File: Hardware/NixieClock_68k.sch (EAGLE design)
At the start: 80 parts, among them IC1 68008, IC10 7805, IC11 MIC803, IC2 AS6C1008, IC3 39SF020, IC4 DS1244Y, IC5 FT245R, IC6 NE555, IC7 ATF1504AS, IC8 74HC377N, IC9 74HC373N, Q1 2N4401

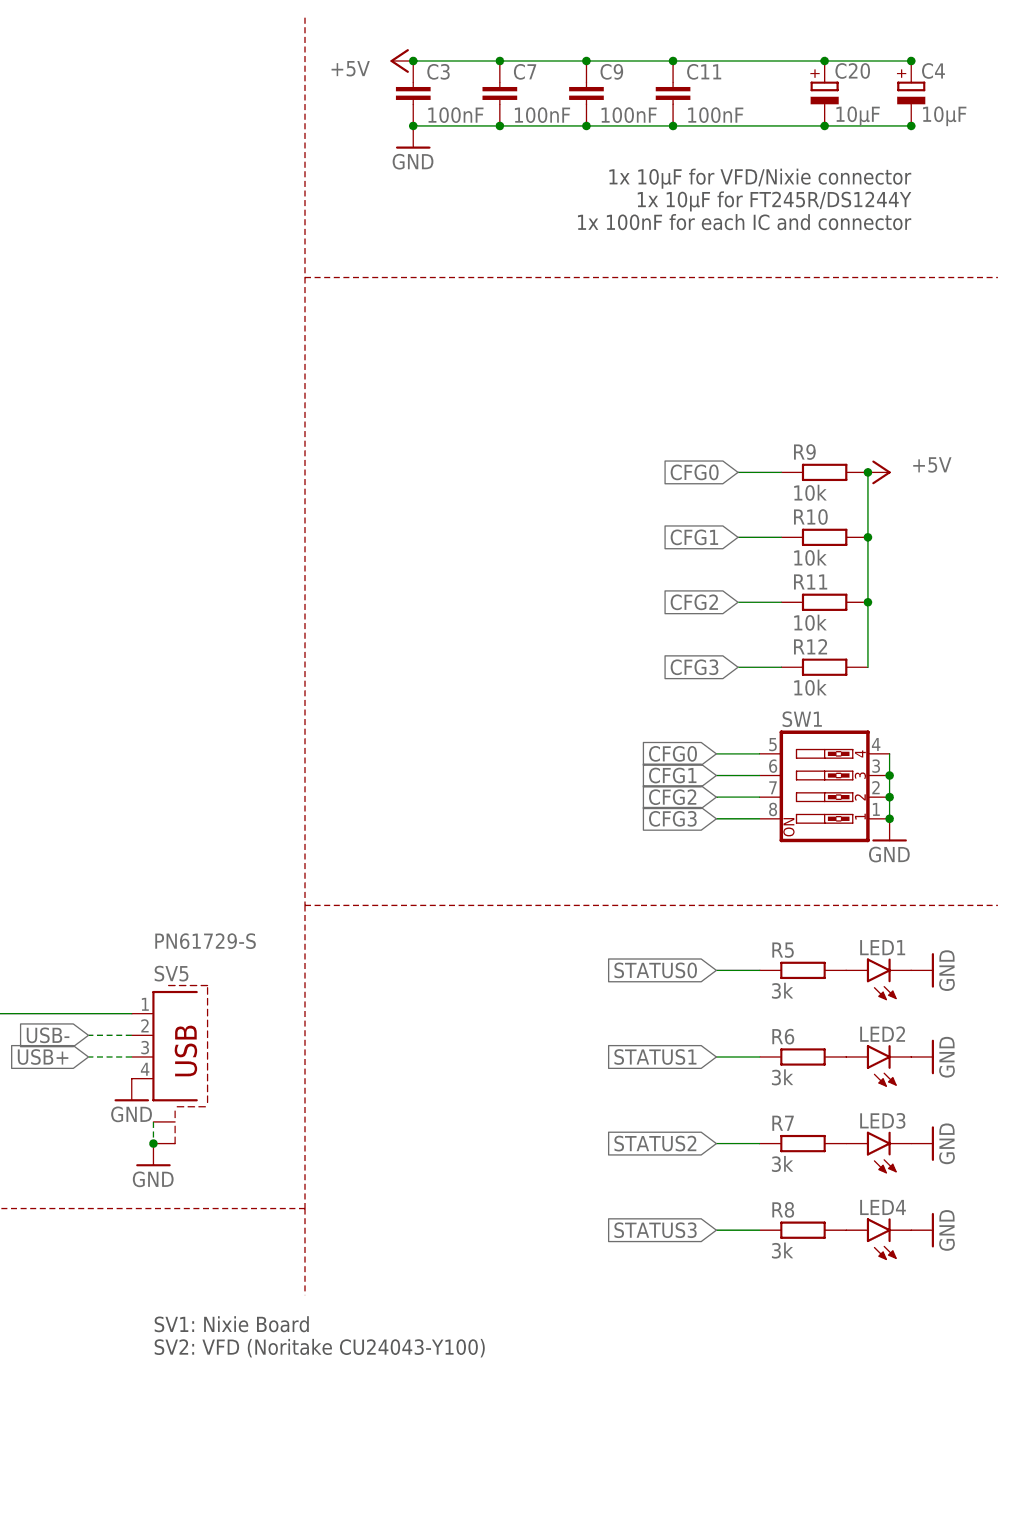
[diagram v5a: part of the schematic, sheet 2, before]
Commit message: more progress routing board
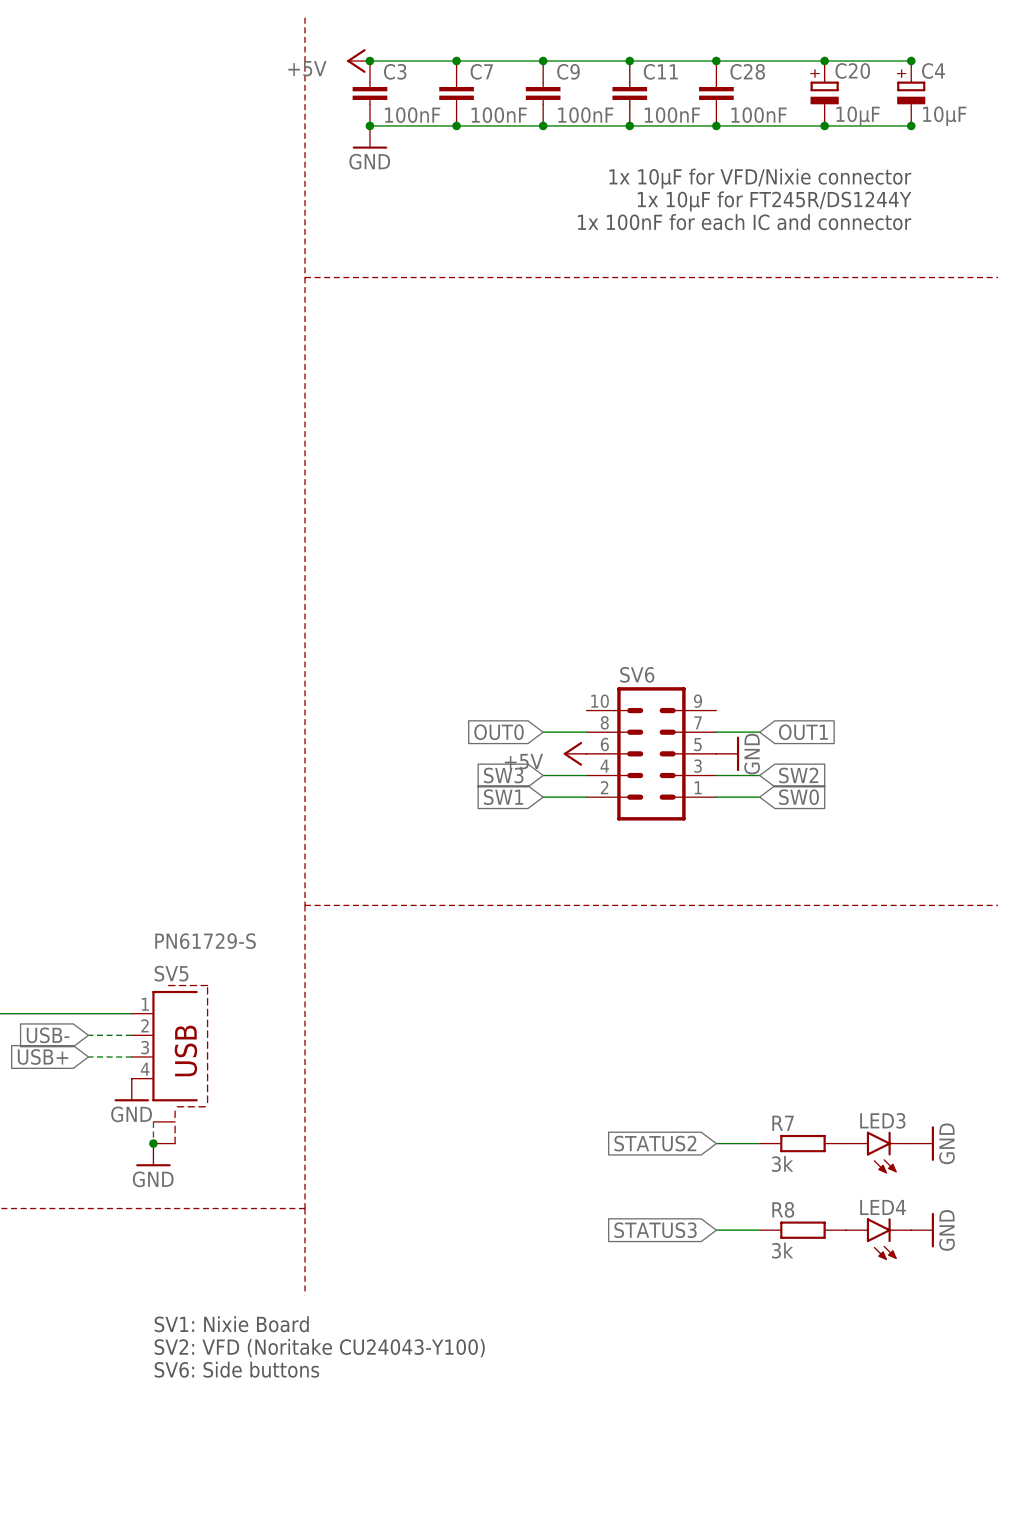
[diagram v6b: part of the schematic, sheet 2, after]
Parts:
- removed D1: 1N4148, diode:1N4148DO35-7
- removed LED1, LED2: (no value), led:LEDCHIPLED_1206
- removed Q1: 2N4401, transistor-npn:2N4416
- removed R10, R11, R12, R9: 10k, rcl:R-EU_R2012
- removed R24, R25: 1k, rcl:R-EU_R2012
- removed R5, R6: 3k, rcl:R-EU_R2012
- removed SP1: KSS1201, buzzer:KSS1201
- removed SW1: (no value), special:SW_DIP-4
- added C28: 100nF, rcl:C-EUC0805
- added SV6: (no value), con-lstb:MA05-2
- renumbered QG1 to X1
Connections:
- removed net !IO_OUT_EN: IC7.IO25
- removed net BEEPER: IC8A.7Q, R24.1
- removed net CFG0: IC9A.5D, R9.1, SW1.5
- removed net CFG1: IC9A.6D, R10.1, SW1.6
- removed net CFG2: IC9A.7D, R11.1, SW1.7
- removed net CFG3: IC9A.8D, R12.1, SW1.8
- removed net JTAG_TCK: IC7.TCK
- removed net JTAG_TDI: IC7.TDI
- removed net JTAG_TDO: IC7.TDO
- removed net JTAG_TMS: IC7.TMS
- removed net N$11: Q1.B, R24.2
- removed net N$12: D1.A, Q1.C, SP1.2
- removed net N$13: D1.C, R25.1
- removed net N$3: LED1.A, R5.2
- removed net N$5: LED2.A, R6.2
- removed net VPA: R22.1
- new net OUT0: IC8A.7Q, SV6.8
- new net OUT1: IC8A.6Q, SV6.7
- new net SW0: IC9A.5D, SV6.1
- new net SW1: IC9A.6D, SV6.2
- new net SW2: IC9A.7D, SV6.3
- new net SW3: IC9A.8D, SV6.4
- net !IO_OUT_CS: now also IC7.IO25
- net !VPA: now also R22.1
- net +5V: now also C28.1, SV6.6; no longer R10.2, R11.2, R12.2, R25.2, R9.2, SP1.1
- net CPLD_TCK: now also IC7.TCK
- net CPLD_TDI: now also IC7.TDI
- net CPLD_TDO: now also IC7.TDO
- net CPLD_TMS: now also IC7.TMS
- net D0: now also SV1.8; no longer SV1.4
- net D2: now also SV1.4; no longer SV1.8
- net GND: now also C28.2, IC9A.4D, SV6.5; no longer LED1.C, LED2.C, Q1.E, SW1.1, SW1.2, SW1.3, SW1.4
- net STATUS0: no longer R5.1
- net STATUS1: no longer R6.1
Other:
- note added: "SV1: Nixie Board SV2: VFD (Noritake CU24043-Y100) SV6: Side buttons"
- note removed: "SV1: Nixie Board SV2: VFD (Noritake CU24043-Y100)"
- moved on the sheet: C11, C3, C7, C9

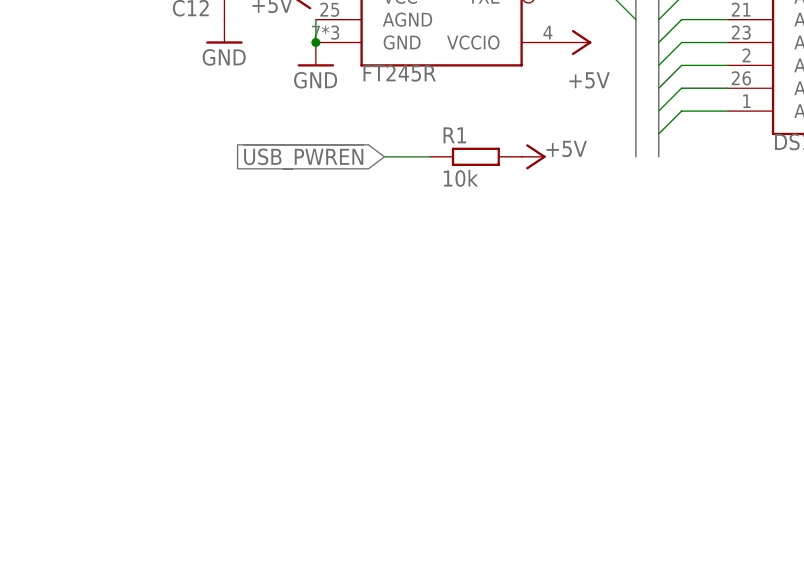
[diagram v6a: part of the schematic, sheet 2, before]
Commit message: added some more missing pull resistors for usb
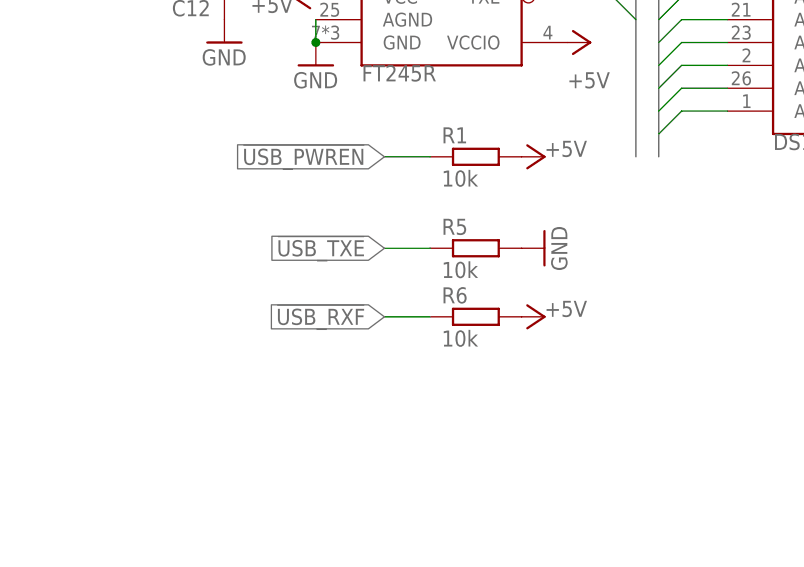
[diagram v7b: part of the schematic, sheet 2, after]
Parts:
- added R5, R6: 10k, rcl:R-EU_R2012
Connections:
- net !USB_RXF: now also R6.1
- net !USB_TXE: now also R5.1
- net +5V: now also R6.2
- net GND: now also R5.2
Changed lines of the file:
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@@
 <part name="P+23" library="supply1" library_urn="urn:adsk.eagle:library:371" deviceset="+5V" device=""/>
 <part name="GND24" library="supply1" library_urn="urn:adsk.eagle:library:371" deviceset="GND" device=""/>
+<part name="R5" library="rcl" library_urn="urn:adsk.eagle:library:334" deviceset="R-EU_" device="R2012" package3d_urn="urn:adsk.eagle:package:23543/2" value="10k">
+<spice>
+<pinmapping spiceprefix="R">
+<pinmap gate="G$1" pin="1" pinorder="1"/>
+<pinmap gate="G$1" pin="2" pinorder="2"/>
+</pinmapping>
+</spice>
+<attribute name="MOUSER" value="652-CR0805FX-1002ELF"/>
+</part>
+<part name="R6" library="rcl" library_urn="urn:adsk.eagle:library:334" deviceset="R-EU_" device="R2012" package3d_urn="urn:adsk.eagle:package:23543/2" value="10k">
+<spice>
+<pinmapping spiceprefix="R">
+<pinmap gate="G$1" pin="1" pinorder="1"/>
+<pinmap gate="G$1" pin="2" pinorder="2"/>
+</pinmapping>
+</spice>
+<attribute name="MOUSER" value="652-CR0805FX-1002ELF"/>
+</part>
+<part name="GND27" library="supply1" library_urn="urn:adsk.eagle:library:371" deviceset="GND" device=""/>
+<part name="P+30" library="supply1" library_urn="urn:adsk.eagle:library:371" deviceset="+5V" device=""/>
 </parts>
 <sheets>
@@
 <attribute name="VALUE" x="195.58" y="99.06" size="1.778" layer="96" rot="R180"/>
 </instance>
+<instance part="R5" gate="G$1" x="50.8" y="109.22" smashed="yes">
+<attribute name="NAME" x="46.99" y="110.7186" size="1.778" layer="95"/>
+<attribute name="VALUE" x="46.99" y="105.918" size="1.778" layer="96"/>
+<attribute name="MOUSER" x="50.8" y="109.22" size="1.778" layer="96" align="top-left" display="off"/>
+</instance>
+<instance part="R6" gate="G$1" x="50.8" y="101.6" smashed="yes">
+<attribute name="NAME" x="46.99" y="103.0986" size="1.778" layer="95"/>
+<attribute name="VALUE" x="46.99" y="98.298" size="1.778" layer="96"/>
+<attribute name="MOUSER" x="50.8" y="101.6" size="1.778" layer="96" align="top-left" display="off"/>
+</instance>
+<instance part="GND27" gate="1" x="58.42" y="109.22" smashed="yes" rot="R90">
+<attribute name="VALUE" x="60.96" y="106.68" size="1.778" layer="96" rot="R90"/>
+</instance>
+<instance part="P+30" gate="1" x="58.42" y="101.6" smashed="yes" rot="R270">
+<attribute name="VALUE" x="58.42" y="101.6" size="1.778" layer="96"/>
+</instance>
 </instances>
 <busses>
@@
 <pinref part="P+23" gate="1" pin="+5V"/>
 </segment>
+<segment>
+<pinref part="R6" gate="G$1" pin="2"/>
+<pinref part="P+30" gate="1" pin="+5V"/>
+</segment>
 </net>
 <net name="GND" class="0">
@@
 <pinref part="GND23" gate="1" pin="GND"/>
 </segment>
+<segment>
+<pinref part="R5" gate="G$1" pin="2"/>
+<pinref part="GND27" gate="1" pin="GND"/>
+</segment>
 </net>
 <net name="!NIXIE_CS" class="0">
@@
 <wire x1="66.04" y1="139.7" x2="68.58" y2="137.16" width="0.1524" layer="91"/>
 </segment>
+<segment>
+<pinref part="R6" gate="G$1" pin="1"/>
+<wire x1="45.72" y1="101.6" x2="40.64" y2="101.6" width="0.1524" layer="91"/>
+<label x="40.64" y="101.6" size="1.778" layer="95" rot="R180" xref="yes"/>
+</segment>
 </net>
 <net name="!USB_TXE" class="0">
@@
 <wire x1="66.04" y1="137.16" x2="68.58" y2="134.62" width="0.1524" layer="91"/>
 </segment>
-</net>
+<segment>
+<pinref part="R5" gate="G$1" pin="1"/>
+<wire x1="45.72" y1="109.22" x2="40.64" y2="109.22" width="0.1524" layer="91"/>
+<label x="40.64" y="109.22" size="1.778" layer="95" rot="R180" xref="yes"/>
+</segment>
+</net>

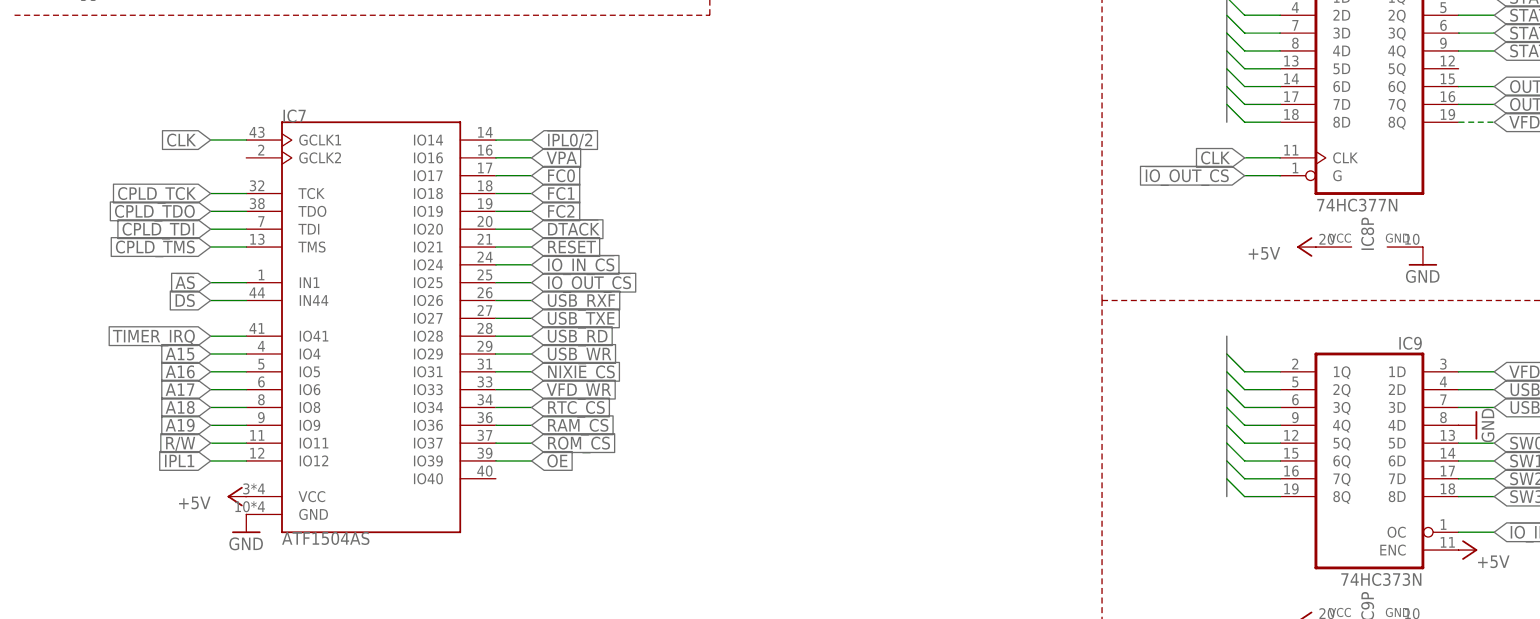
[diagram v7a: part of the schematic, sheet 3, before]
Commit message: more routing of address bus
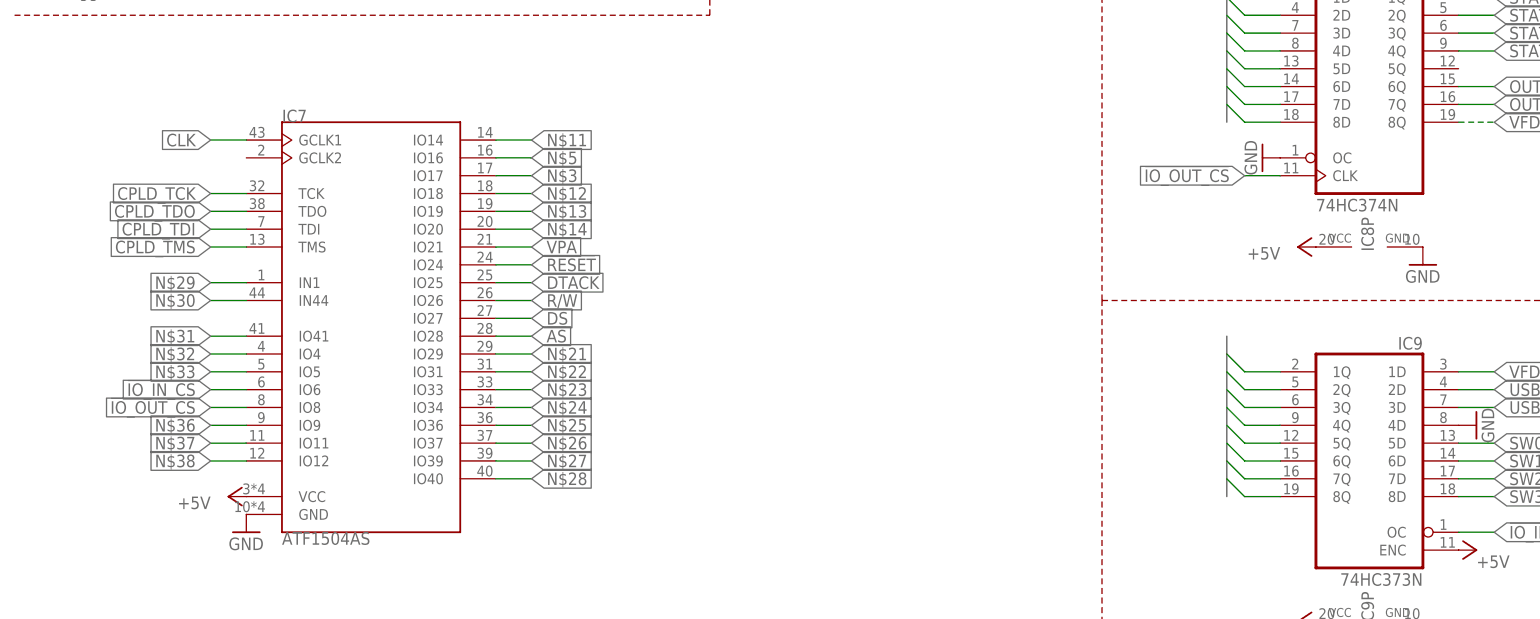
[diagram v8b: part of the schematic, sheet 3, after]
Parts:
- IC8: value 74HC377N -> 74HC374N; device 74xx-eu:74HC377N -> 74xx-eu:74HC374N; MOUSER 595-SN74HC377N -> 595-SN74HC574N
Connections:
- new net N$11: IC7.IO14
- new net N$12: IC7.IO18
- new net N$13: IC7.IO19
- new net N$14: IC7.IO20
- new net N$21: IC7.IO29
- new net N$22: IC7.IO31
- new net N$23: IC7.IO33
- new net N$24: IC7.IO34
- new net N$25: IC7.IO36
- new net N$26: IC7.IO37
- new net N$27: IC7.IO39
- new net N$28: IC7.IO40
- new net N$29: IC7.IN1
- new net N$3: IC7.IO17
- new net N$30: IC7.IN44
- new net N$31: IC7.IO41
- new net N$32: IC7.IO4
- new net N$33: IC7.IO5
- new net N$36: IC7.IO9
- new net N$37: IC7.IO11
- new net N$38: IC7.IO12
- new net N$5: IC7.IO16
- net !AS: now also IC7.IO28; no longer IC7.IN1, SV1.15
- net !DS: now also IC7.IO27; no longer IC7.IN44
- net !DTACK: now also IC7.IO25; no longer IC7.IO20
- net !IO_IN_CS: now also IC7.IO6; no longer IC7.IO24
- net !IO_OUT_CS: now also IC7.IO8, IC8A.CLK; no longer IC7.IO25, IC8A.G
- net !IPL0/2: no longer IC7.IO14
- net !IPL1: no longer IC7.IO12
- net !NIXIE_CS: no longer IC7.IO31
- net !OE: no longer IC7.IO39
- net !RAM_CS: no longer IC7.IO36
- net !RESET: now also IC7.IO24; no longer IC7.IO21
- net !ROM_CS: no longer IC7.IO37
- net !RTC_CS: no longer IC7.IO34
- net !USB_RD: no longer IC7.IO28
- net !USB_RXF: no longer IC7.IO26
- net !USB_TXE: no longer IC7.IO27
- net !VFD_WR: no longer IC7.IO33
- net !VPA: now also IC7.IO21; no longer IC7.IO16
- net A15: no longer IC7.IO4
- net A16: no longer IC7.IO5
- net A17: no longer IC7.IO6
- net A18: no longer IC7.IO8
- net A19: no longer IC7.IO9
- net CLK: no longer IC8A.CLK
- net FC0: no longer IC7.IO17
- net FC1: no longer IC7.IO18
- net FC2: no longer IC7.IO19
- net GND: now also IC8A.OC
- net R/!W!: now also IC7.IO26; no longer IC7.IO11
- net TIMER_IRQ: no longer IC7.IO41
- net USB_WR: no longer IC7.IO29
